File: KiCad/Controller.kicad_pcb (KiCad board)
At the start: 2 copper layers, 45 x 45 mm, 38 parts, among them J1 Inputs, J2 POWER, J3 RANGER, J4 RFID, J5 OUT1, J6 OUT2, J7 OUT3, J8 OUT4, J9 USB-C, Q1 BC817, U1 ESP32-WROOM-32, U2 G3VM-41GR8, U3 G3VM-41GR8, U4 G3VM-41GR8, U5 G3VM-41GR8, U6 FT231XQ, U7 QR

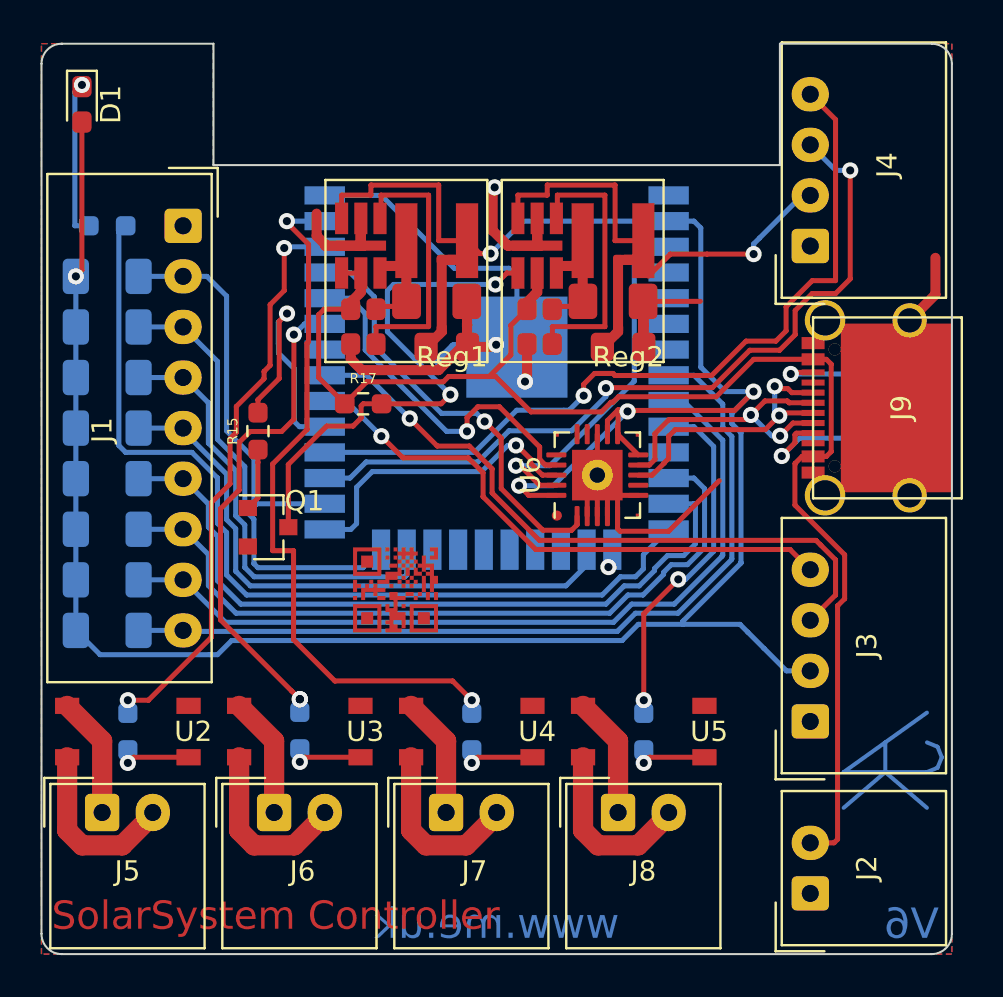
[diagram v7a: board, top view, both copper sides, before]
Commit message: Updated connector models and added 0.1uF
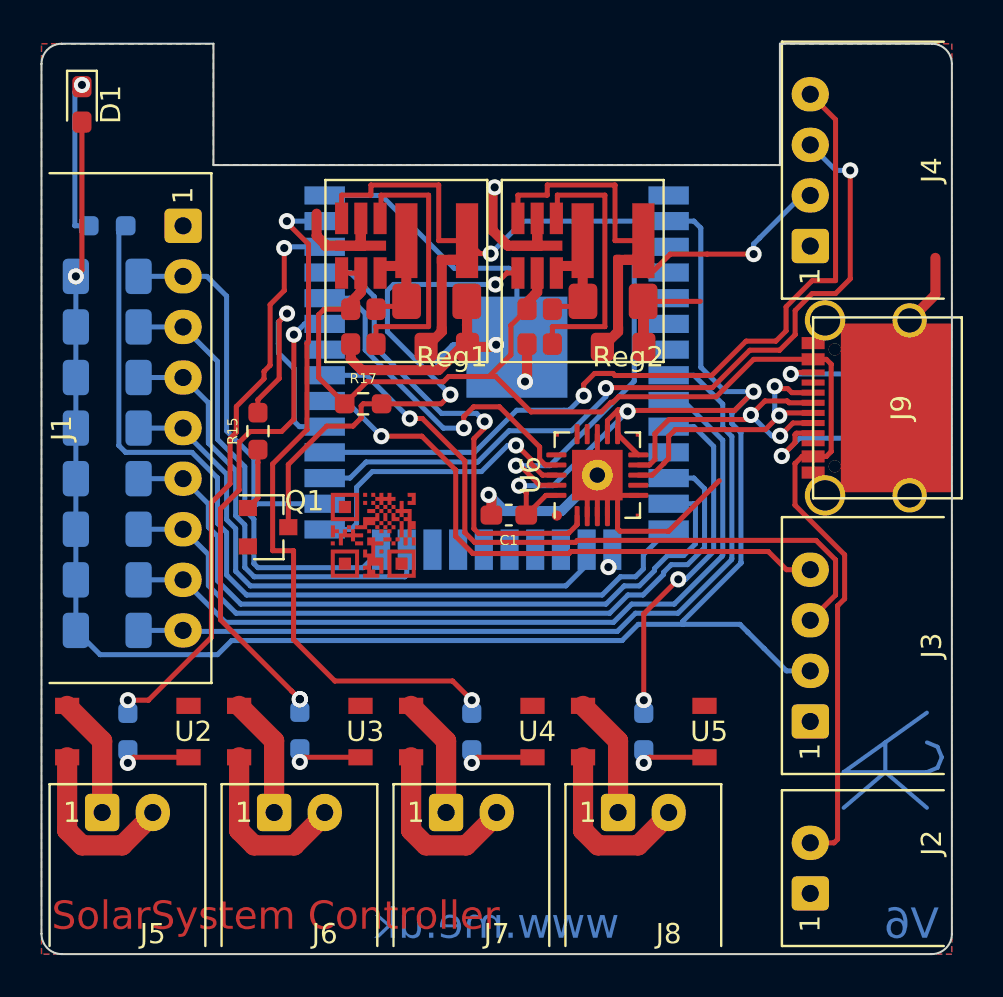
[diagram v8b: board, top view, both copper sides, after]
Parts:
- added C1: 0.1uF, Capacitor_SMD:C_0603_1608Metric_Pad1.08x0.95mm_HandSolder, F.Cu at (73.1, 118.3)
- J1: footprint Connector_Molex:Molex_SPOX_5268-09A_1x09_P2.50mm_Horizontal -> RevK:Molex_MiniSPOX_H9RA
- J2, J5, J6, J7, J8: footprint Connector_Molex:Molex_SPOX_5268-02A_1x02_P2.50mm_Horizontal -> RevK:Molex_MiniSPOX_H2RA
- J3, J4: footprint Connector_Molex:Molex_SPOX_5268-04A_1x04_P2.50mm_Horizontal -> RevK:Molex_MiniSPOX_H4RA
- moved J1 10.0 mm to (57.0, 114.0)
- moved J3 3.75 mm to (88.0, 124.8)
- moved J4 3.75 mm to (88.0, 101.2)
- moved U7 2.92 mm to (66.4, 119.3)
- moved J2 1.25 mm to (88.0, 135.8)
- moved J5 1.25 mm to (54.2, 133.0)
- moved J6 1.25 mm to (62.8, 133.0)
- moved J7 1.25 mm to (71.2, 133.0)
- moved J8 1.25 mm to (79.8, 133.0)
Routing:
- net GND: track 67.9 -> 75.3 mm, vias 4 -> 5
- net O: track 21.2 -> 23.7 mm
- net SCL: track 33.2 -> 34.7 mm
- net +3V3: track 120.4 -> 121.9 mm
- net SDA: track 28.2 -> 29.5 mm
